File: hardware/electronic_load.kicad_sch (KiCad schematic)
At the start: 16 parts, among them J1 Shunt_1, J2 Shunt_2, J3 Gate_Drive, J4 SWD_Debug, SW1 EC11, U1 RaspberryPi_Pico, U2 INA185A1IDBVR, U3 INA185A1IDBVR

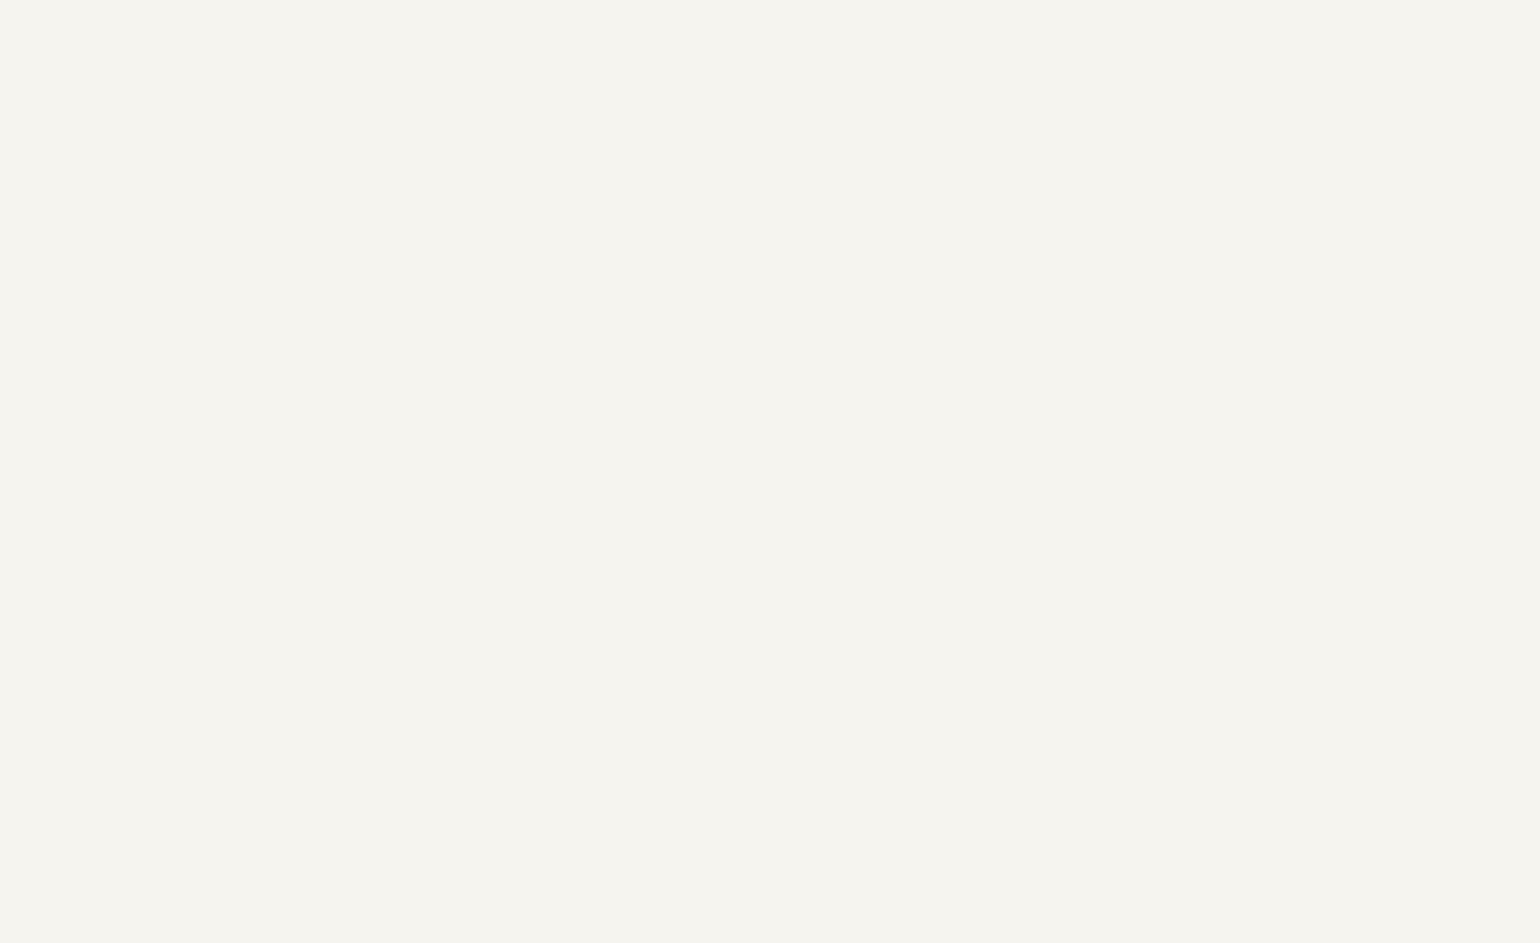
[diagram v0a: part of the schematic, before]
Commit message: hardware: analog frontend — per-FET linear loops, sim workspace, datasheets
Schematic (both gate-buffer variants, as simulated in hardware/sim/):
- Shared setpoint DAC: GATE_PWM -> 2-pole RC -> VSET
- Ch A: OPA192 integrator -> discrete class-AB (BD139/BD140, 1N4148 bias)
  -> 4R7 -> IXFN360N10T -> 2 mOhm Ohmite TGHG shunt (both SOT-227,
  shared heatsink, short bus bars) -> INA185 sense
- Ch B: OPA192 -> BUF634A -> 4R7 -> IXFN360N10T -> TGHG -> INA185
- J5 DUT_BUS drain connector, +15V analog rail
- Tests extended to 11 (analog nets, VDUT bus, both variants present);
  SYMLIB now resolved by glob instead of hardcoded flatpak hash

Simulation workspace (LTspice via wine, validated headless):
- VDMOS model anchored to IXYS DS100088: gfs=160S@60A (Kp=213, Vto=3.8),
  Ciss=36n, Crss=330p, Qg=505n
- AC loop-gain bench (DC-closed/AC-open break): fc=32.6 kHz, PM=81 deg,
  GM=26 dB at 40 A with TGHG 2m + INA185A1
- ltraw.py raw-file parser, make_figs.py figure generator, 4 design figures

Datasheets vendored for cross-reference (IXFN360N10T is the real DS100088,
recovered via Wayback Machine).

Co-Authored-By: Claude Fable 5 <noreply@anthropic.com>
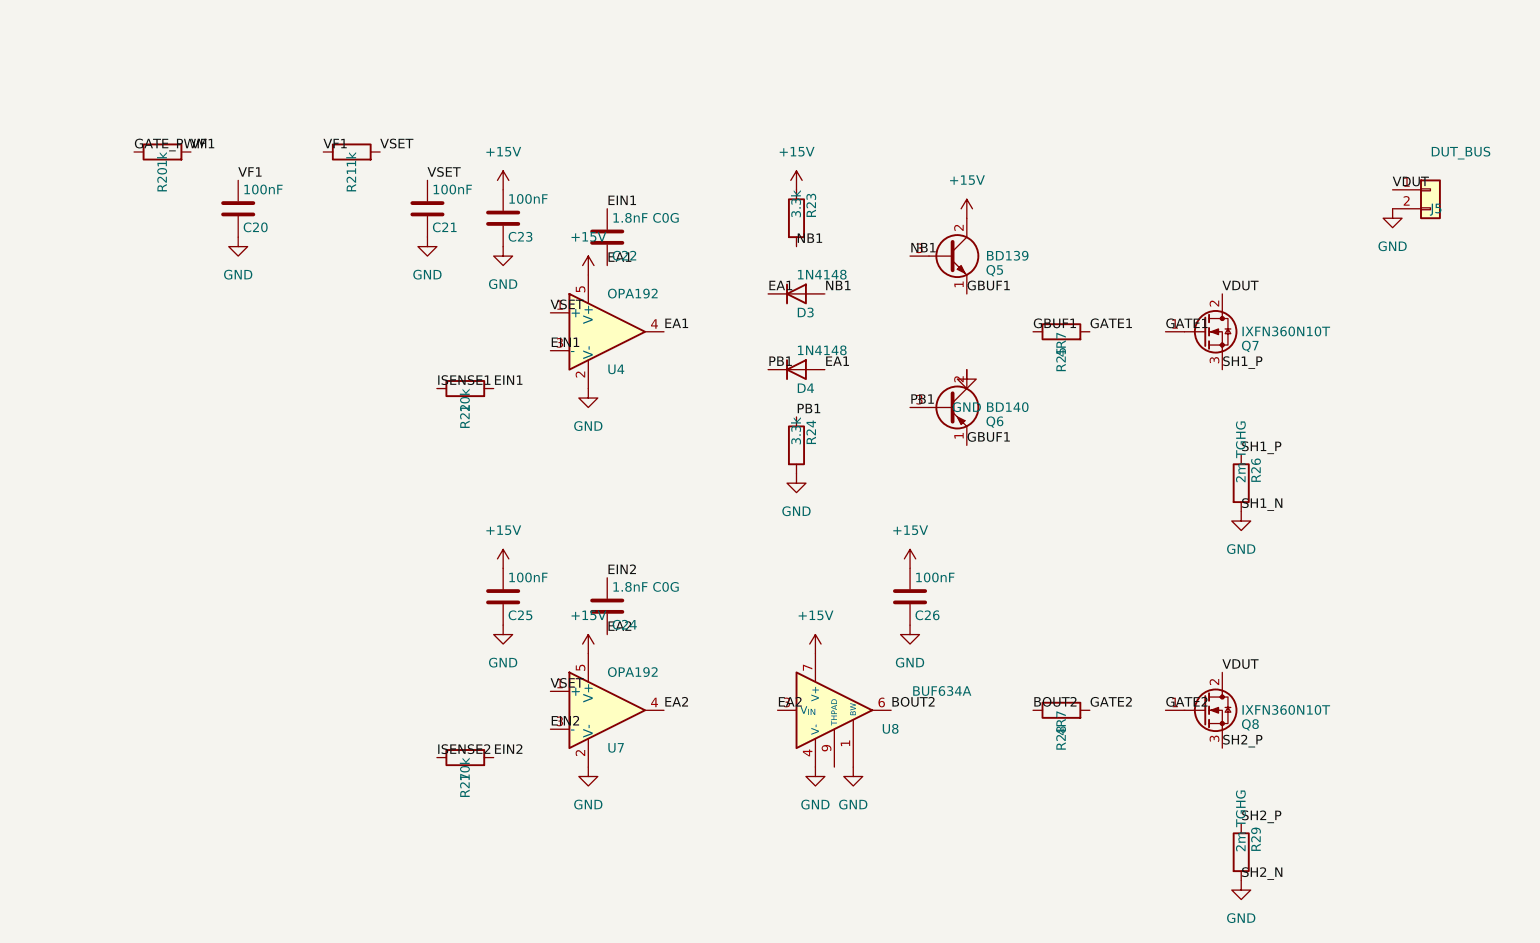
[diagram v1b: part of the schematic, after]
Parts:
- added C20, C21, C23, C25, C26: 100nF, Capacitor_SMD:C_0603_1608Metric, symbol Device:C
- added C22, C24: 1.8nF C0G, Capacitor_SMD:C_0603_1608Metric, symbol Device:C
- added D3, D4: 1N4148, Diode_THT:D_DO-35_SOD27_P7.62mm_Horizontal, symbol Diode:1N4148
- added J5: DUT_BUS, Connector_PinHeader_2.54mm:PinHeader_1x02_P2.54mm_Vertical, symbol Connector_Generic:Conn_01x02
- added Q5: BD139, Package_TO_SOT_THT:TO-126-3_Vertical, symbol Transistor_BJT:BD139
- added Q6: BD140, Package_TO_SOT_THT:TO-126-3_Vertical, symbol Transistor_BJT:BD140
- added Q7, Q8: IXFN360N10T, Package_TO_SOT_THT:SOT-227, symbol Transistor_FET:Q_NMOS_GDS
- added R20, R21: 1k, Resistor_SMD:R_0603_1608Metric, symbol Device:R
- added R22, R27: 10k, Resistor_SMD:R_0603_1608Metric, symbol Device:R
- added R23, R24: 3.3k, Resistor_SMD:R_0603_1608Metric, symbol Device:R
- added R25, R28: 4R7, Resistor_SMD:R_0603_1608Metric, symbol Device:R
- added R26, R29: 2m TGHG, Package_TO_SOT_THT:SOT-227, symbol Device:R
- added U4, U7: OPA192, Package_TO_SOT_SMD:SOT-23-5, symbol Amplifier_Operational:LMV321
- added U8: BUF634A, Package_SO:HSOP-8-1EP_3.9x4.9mm_P1.27mm_EP2.41x3.1mm, symbol Amplifier_Buffer:BUF634AxDDA
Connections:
- net SH1_N is gone; now on net GND: J1.3 (Pin_3), U2.4 (-)
- net SH2_N is gone; now on net GND: J2.3 (Pin_3), U3.4 (-)
- net GATE_PWM: now also R20.1
- net GND: now also C20.2, C21.2, C23.2, C25.2, C26.2, J5.2 (Pin_2), Q6.2 (C), R24.2, R26.2, R29.2, U4.2 (V-), U7.2 (V-), U8.1 (BW), U8.4 (V-)
- net ISENSE1: now also R22.1
- net ISENSE2: now also R27.1
- net SH1_P: now also Q7.3 (S), R26.1
- net SH2_P: now also Q8.3 (S), R29.1
- new net +15V: C23.1, C25.1, C26.1, Q5.2 (C), R23.1, U4.5 (V+), U7.5 (V+), U8.7 (V+)
- new net BOUT2: R28.1, U8.6
- new net EA1: C22.2, D3.1 (K), D4.2 (A), U4.4
- new net EA2: C24.2, U7.4, U8.3 (V_{IN})
- new net EIN1: C22.1, R22.2, U4.3 (-)
- new net EIN2: C24.1, R27.2, U7.3 (-)
- new net GATE1: Q7.1 (G), R25.2
- new net GATE2: Q8.1 (G), R28.2
- new net GBUF1: Q5.1 (E), Q6.1 (E), R25.1
- new net NB1: D3.2 (A), Q5.3 (B), R23.2
- new net PB1: D4.1 (K), Q6.3 (B), R24.1
- new net VDUT: J5.1 (Pin_1), Q7.2 (D), Q8.2 (D)
- new net VF1: C20.1, R20.2, R21.1
- new net VSET: C21.1, R21.2, U4.1 (+), U7.1 (+)
